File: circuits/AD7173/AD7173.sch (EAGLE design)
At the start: 32 parts, among them IC1 AD7173, IC2 ADP1720, IC3 ADP1720ARMZ-5, IC4 OPA2134D, IC6 OPA2725DGK

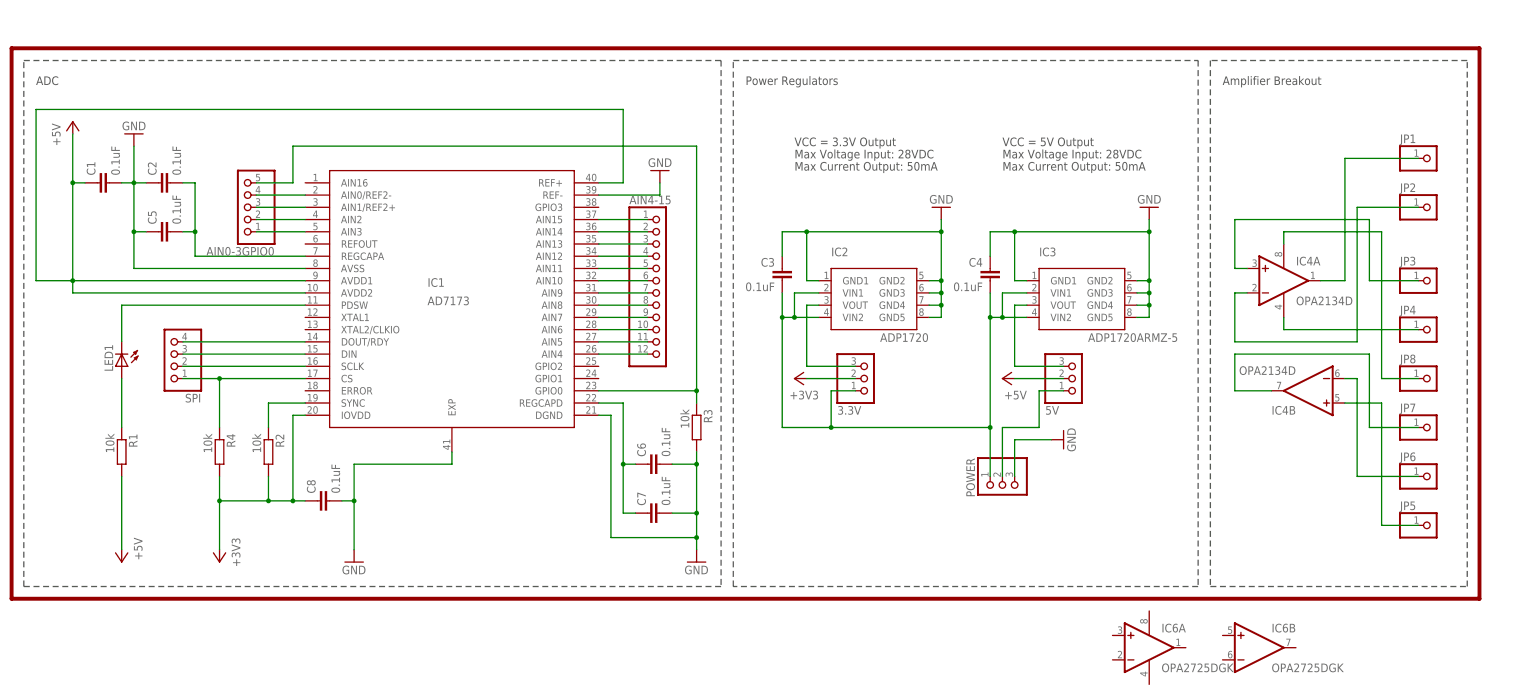
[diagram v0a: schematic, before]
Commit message: upadted AD7173 circuits
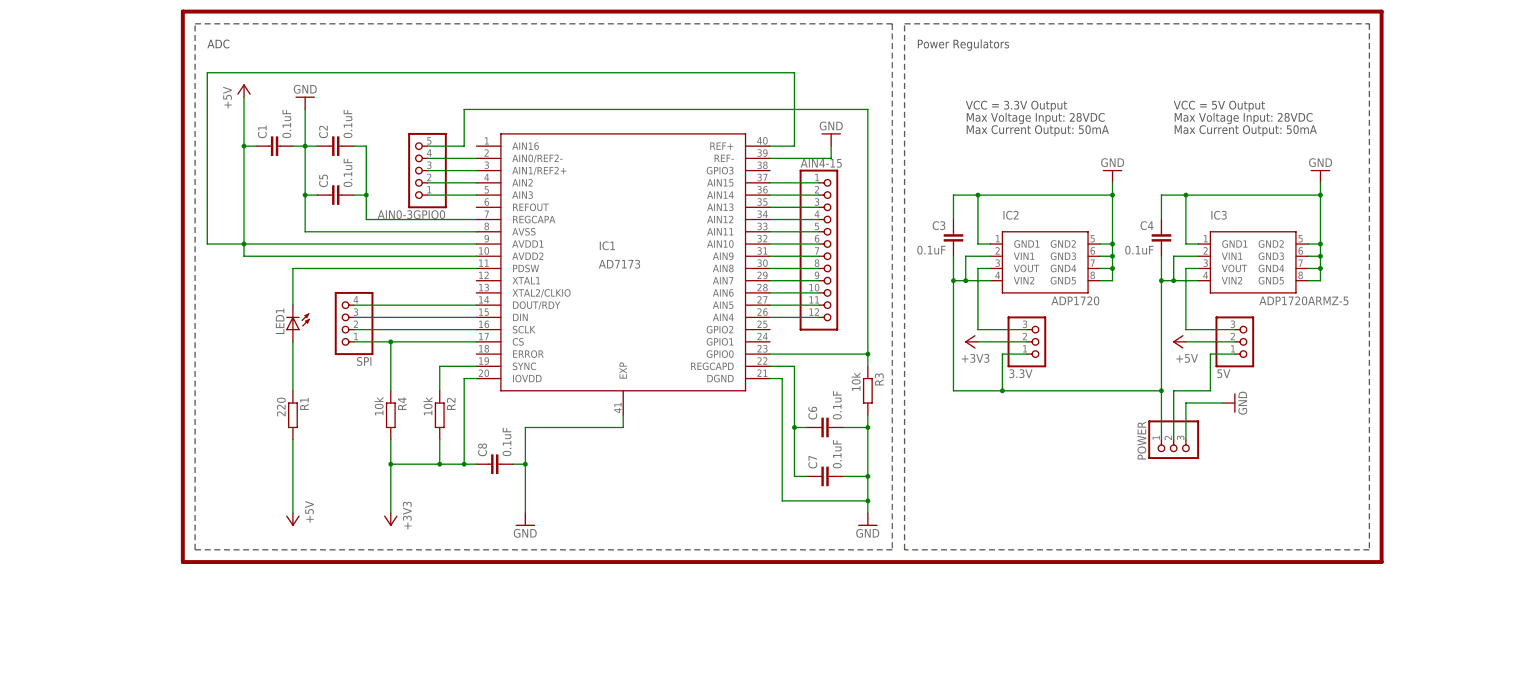
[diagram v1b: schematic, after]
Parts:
- removed IC4: OPA2134D, linear:OPA2134D
- removed IC6: OPA2725DGK, linear:OPA2725DGK
- removed JP1, JP2, JP3, JP4, JP5, JP6, JP7, JP8: (no value), pinhead:PINHD-1X1
- R1: value 10k -> 220
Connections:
- removed net N$31: IC4A.OUT, JP1.1
- removed net N$33: IC4A.-IN, JP2.1
- removed net N$34: IC4A.+IN, JP3.1
- removed net N$35: IC4P.V-, JP4.1
- removed net N$36: IC4B.+IN, JP5.1
- removed net N$37: IC4B.-IN, JP6.1
- removed net N$40: IC4B.OUT, JP7.1
- removed net N$41: IC4P.V+, JP8.1
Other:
- note removed: "Amplifier Breakout"
- moved on the sheet: 3.3V, 5V, AIN0-3GPIO0, AIN4-15, C1, C2, C3, C4, C5, C6, C7, C8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

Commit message: updated AD7173 circuit
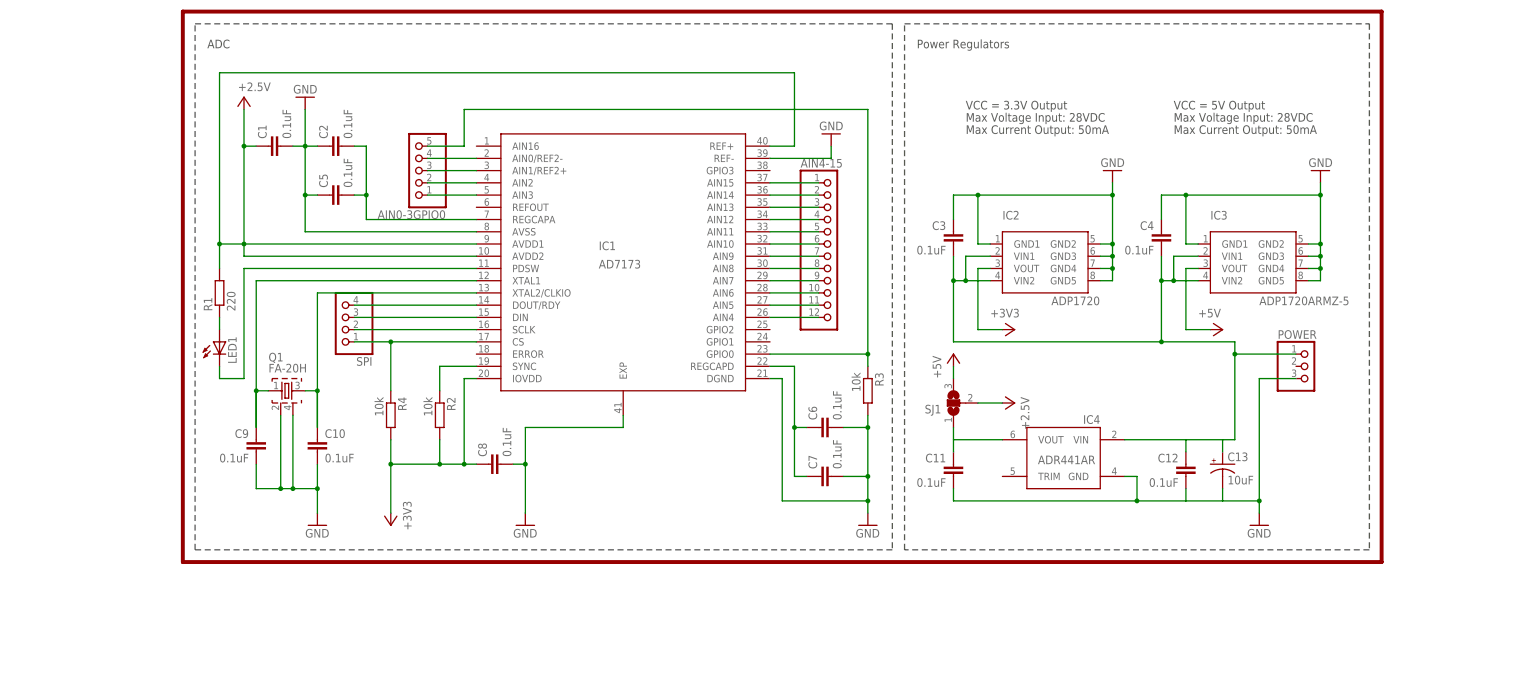
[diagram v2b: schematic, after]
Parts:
- removed 3.3V, 5V: (no value), pinhead:PINHD-1X3
- added C10, C11, C12, C9: 0.1uF, rcl:C-EUC0402
- added C13: 10uF, rcl:CPOL-USE1.8-4
- added IC4: ADR441AR, kblom:ADR441AR
- added Q1: FA-20H, crystal:FA-20H
- added SJ1: (no value), jumper:SJ2W
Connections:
- removed net N$30: 5V.3, IC3.VOUT
- new net V+: C1.1, IC1.AVDD1, IC1.AVDD2, IC1.REF+, R1.2, SJ1.2
- new net VIN: C12.1, C13.+, C3.2, C4.2, IC2.VIN1, IC2.VIN2, IC3.VIN1, IC3.VIN2, IC4.VIN, POWER.1
- net +3V3: now also IC2.VOUT; no longer 3.3V.2
- net +5V: now also IC3.VOUT, SJ1.3; no longer 5V.2, C1.1, IC1.AVDD1, IC1.AVDD2, IC1.REF+, R1.2
- net GND: now also C10.2, C11.2, C12.2, C13.-, C9.2, IC4.GND, Q1.2, Q1.4
- net N$22: now also C10.1, IC1.XTAL2/CLKIO, Q1.3; no longer 5V.1, POWER.2
- net N$27: now also C9.1, IC1.XTAL1, Q1.1; no longer 3.3V.3, IC2.VOUT
- net N$28: now also C11.1, IC4.VOUT, SJ1.1; no longer 3.3V.1, C3.2, C4.2, IC2.VIN1, IC2.VIN2, IC3.VIN1, IC3.VIN2, POWER.1
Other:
- moved on the sheet: LED1, POWER, R1

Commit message: updated AD7173 breakout board
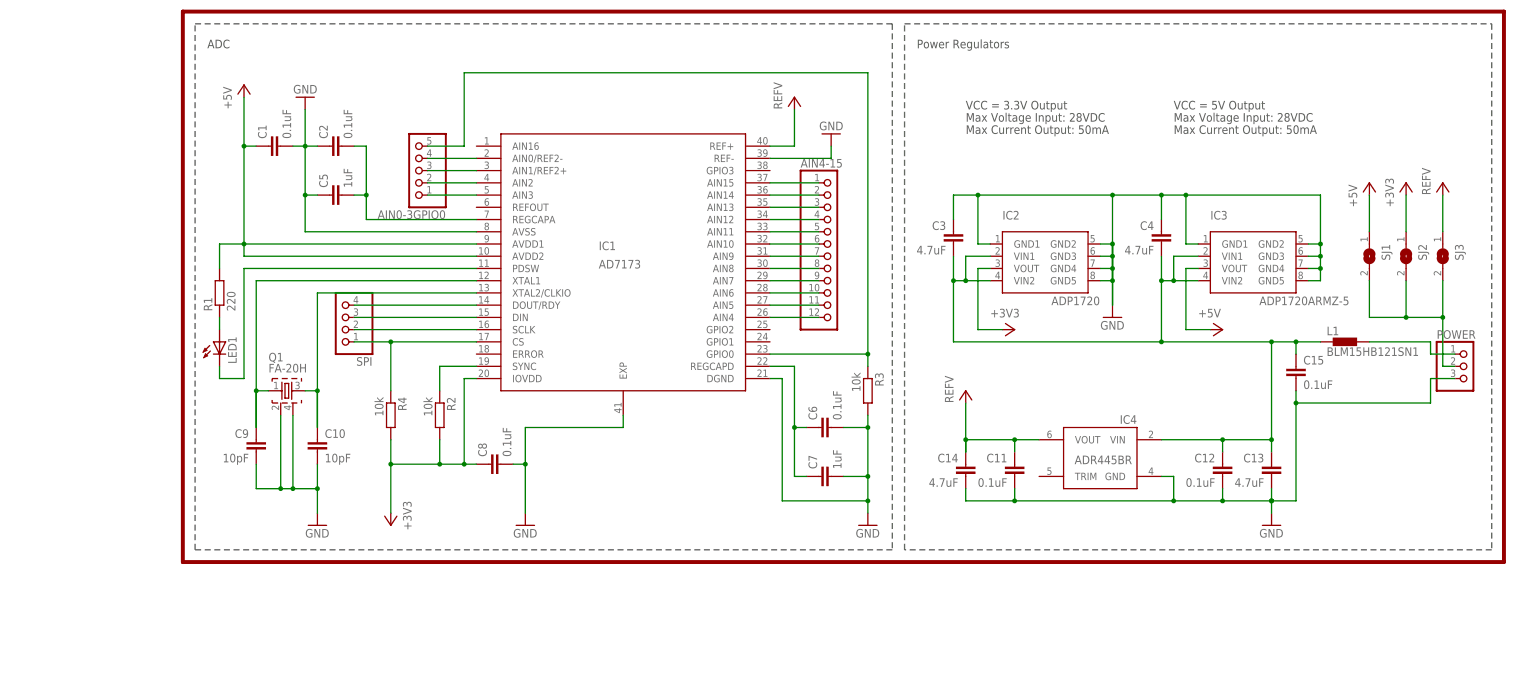
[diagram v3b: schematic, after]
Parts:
- added C14: 4.7uF, rcl:C-EUC0402
- added C15: 0.1uF, rcl:C-EUC0402
- added L1: BLM15HB121SN1, inductors:BLM15HB121SN1
- added SJ2, SJ3: (no value), jumper:SJ
- C10, C9: value 0.1uF -> 10pF
- C13: value 10uF -> 4.7uF; device rcl:CPOL-USE1.8-4 -> rcl:C-EUC0402
- C3, C4: value 0.1uF -> 4.7uF
- C5, C7: value 0.1uF -> 1uF
- IC4: value ADR441AR -> ADR445BR; device kblom:ADR441AR -> kblom:ADR445BR
- SJ1: device jumper:SJ2W -> jumper:SJ
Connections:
- removed net V+: C1.1, IC1.AVDD1, IC1.AVDD2, IC1.REF+, R1.2, SJ1.2
- new net N$30: L1.2, POWER.1
- new net VCC: C11.1, C14.1, IC1.REF+, IC4.VOUT, SJ3.1
- net +3V3: now also SJ2.1
- net +5V: now also C1.1, IC1.AVDD1, IC1.AVDD2, R1.2, SJ1.1; no longer SJ1.3
- net GND: now also C13.2, C14.2, C15.2; no longer C13.-
- net N$28: now also POWER.2, SJ1.2, SJ2.2, SJ3.2; no longer C11.1, IC4.VOUT, SJ1.1
- net VIN: now also C13.1, C15.1, L1.1; no longer C13.+, POWER.1
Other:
- moved on the sheet: C11, C12, IC4, POWER

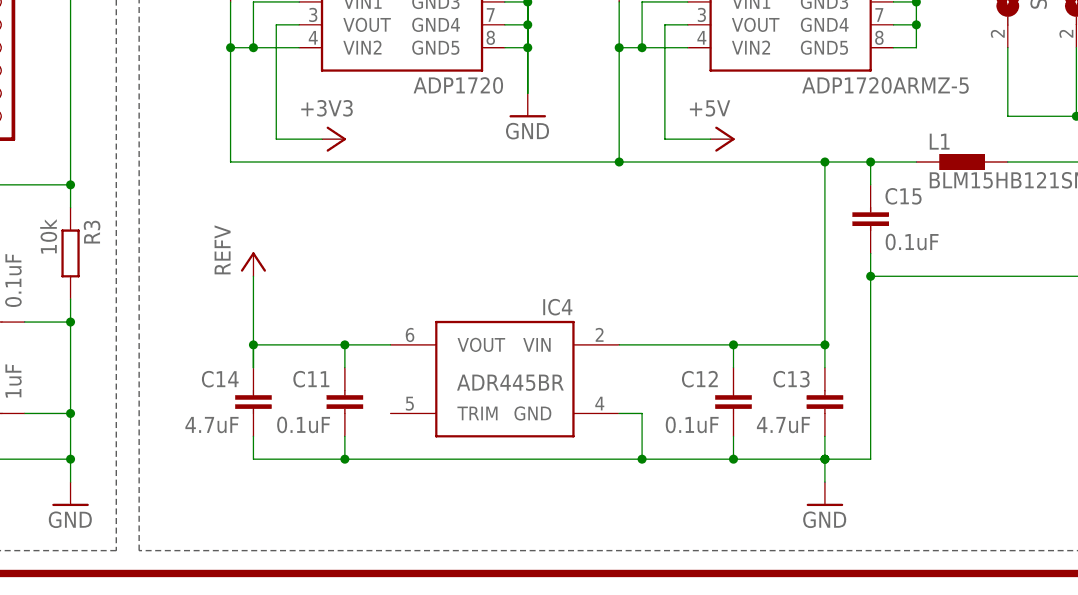
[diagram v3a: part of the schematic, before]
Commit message: updated AD7173 breakout board
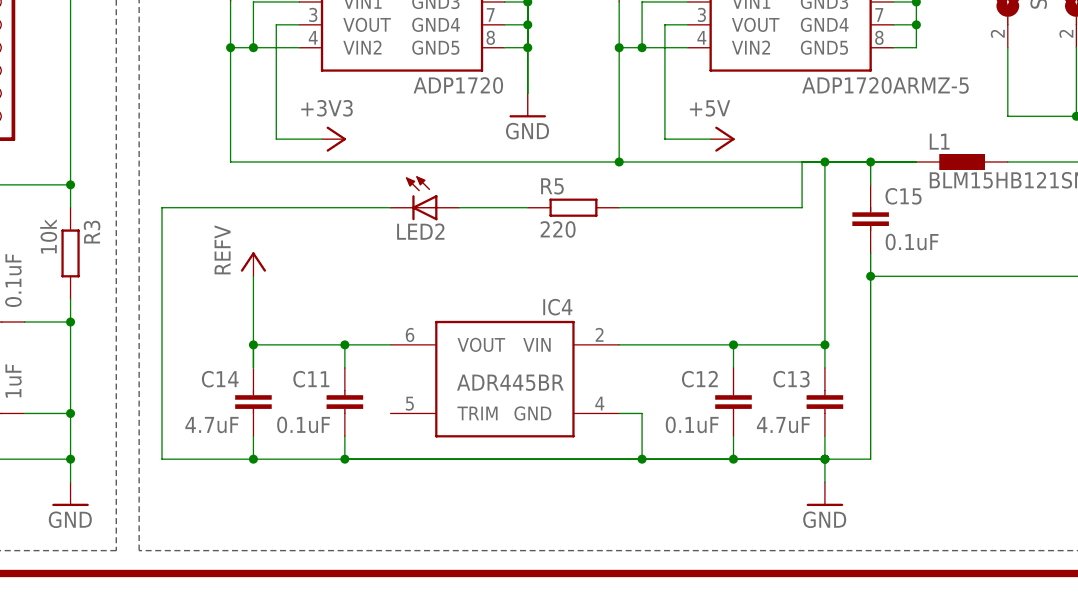
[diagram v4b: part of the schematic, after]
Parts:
- added LED2: (no value), led:LEDCHIP-LED0603
- added R5: 220, rcl:R-EU_R0402
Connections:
- new net N$31: LED2.A, R5.1
- net GND: now also LED2.C
- net VIN: now also R5.2
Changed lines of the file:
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@@
 <part name="+3V3" library="supply1" deviceset="+3V3" device=""/>
 <part name="P+6" library="supply1" deviceset="VCC" device="" value="REFV"/>
+<part name="LED2" library="led" deviceset="LED" device="CHIP-LED0603"/>
+<part name="R5" library="rcl" deviceset="R-EU_" device="R0402" value="220"/>
 </parts>
 <sheets>
@@
 <instance part="+3V3" gate="G$1" x="254" y="78.74"/>
 <instance part="P+6" gate="VCC" x="261.62" y="78.74"/>
+<instance part="LED2" gate="G$1" x="182.88" y="40.64" rot="R270"/>
+<instance part="R5" gate="G$1" x="198.12" y="40.64"/>
 </instances>
 <busses>
@@
 <wire x1="215.9" y1="12.7" x2="226.06" y2="12.7" width="0.1524" layer="91"/>
 <wire x1="226.06" y1="15.24" x2="226.06" y2="12.7" width="0.1524" layer="91"/>
-<wire x1="226.06" y1="12.7" x2="226.06" y2="10.16" width="0.1524" layer="91"/>
 <pinref part="C13" gate="G$1" pin="2"/>
 <junction x="215.9" y="12.7"/>
@@
 <wire x1="231.14" y1="33.02" x2="231.14" y2="35.56" width="0.1524" layer="91"/>
 <junction x="172.72" y="12.7"/>
+<pinref part="LED2" gate="G$1" pin="C"/>
+<wire x1="177.8" y1="40.64" x2="152.4" y2="40.64" width="0.1524" layer="91"/>
+<wire x1="152.4" y1="40.64" x2="152.4" y2="12.7" width="0.1524" layer="91"/>
+<wire x1="152.4" y1="12.7" x2="162.56" y2="12.7" width="0.1524" layer="91"/>
+<wire x1="172.72" y1="12.7" x2="226.06" y2="12.7" width="0.1524" layer="91"/>
+<wire x1="226.06" y1="12.7" x2="226.06" y2="10.16" width="0.1524" layer="91"/>
+<junction x="162.56" y="12.7"/>
 </segment>
 <segment>
@@
 <junction x="226.06" y="45.72"/>
 <junction x="231.14" y="45.72"/>
+<wire x1="236.22" y1="45.72" x2="223.52" y2="45.72" width="0.1524" layer="91"/>
+<wire x1="223.52" y1="45.72" x2="223.52" y2="40.64" width="0.1524" layer="91"/>
+<pinref part="R5" gate="G$1" pin="2"/>
+<wire x1="223.52" y1="40.64" x2="203.2" y2="40.64" width="0.1524" layer="91"/>
 </segment>
 </net>
@@
 </segment>
 </net>
+<net name="N$31" class="0">
+<segment>
+<pinref part="LED2" gate="G$1" pin="A"/>
+<pinref part="R5" gate="G$1" pin="1"/>
+<wire x1="193.04" y1="40.64" x2="185.42" y2="40.64" width="0.1524" layer="91"/>
+</segment>
+</net>

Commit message: upadted AD7173 breakout board
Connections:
- net N$30: now also R5.2
- net VIN: no longer R5.2
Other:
- moved on the sheet: C15, L1
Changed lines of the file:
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@@
 <instance part="P+2" gate="VCC" x="127" y="96.52"/>
 <instance part="P+1" gate="VCC" x="162.56" y="35.56"/>
-<instance part="L1" gate="G$1" x="241.3" y="45.72"/>
-<instance part="C15" gate="G$1" x="231.14" y="40.64"/>
+<instance part="L1" gate="G$1" x="241.3" y="43.18"/>
+<instance part="C15" gate="G$1" x="231.14" y="38.1"/>
 <instance part="P+4" gate="1" x="12.7" y="99.06"/>
 <instance part="SJ1" gate="1" x="246.38" y="63.5" rot="R270"/>
@@
 <pinref part="GND5" gate="1" pin="GND"/>
 <wire x1="226.06" y1="12.7" x2="231.14" y2="12.7" width="0.1524" layer="91"/>
-<wire x1="231.14" y1="12.7" x2="231.14" y2="33.02" width="0.1524" layer="91"/>
+<wire x1="231.14" y1="12.7" x2="231.14" y2="30.48" width="0.1524" layer="91"/>
 <pinref part="IC4" gate="G$1" pin="GND"/>
 <pinref part="C11" gate="G$1" pin="2"/>
@@
 <wire x1="162.56" y1="12.7" x2="172.72" y2="12.7" width="0.1524" layer="91"/>
 <wire x1="172.72" y1="12.7" x2="172.72" y2="15.24" width="0.1524" layer="91"/>
-<junction x="231.14" y="33.02"/>
+<junction x="231.14" y="30.48"/>
 <wire x1="264.16" y1="38.1" x2="259.08" y2="38.1" width="0.1524" layer="91"/>
-<wire x1="259.08" y1="38.1" x2="259.08" y2="33.02" width="0.1524" layer="91"/>
+<wire x1="259.08" y1="38.1" x2="259.08" y2="30.48" width="0.1524" layer="91"/>
 <pinref part="C15" gate="G$1" pin="2"/>
-<wire x1="259.08" y1="33.02" x2="231.14" y2="33.02" width="0.1524" layer="91"/>
-<wire x1="231.14" y1="33.02" x2="231.14" y2="35.56" width="0.1524" layer="91"/>
+<wire x1="259.08" y1="30.48" x2="231.14" y2="30.48" width="0.1524" layer="91"/>
+<wire x1="231.14" y1="30.48" x2="231.14" y2="33.02" width="0.1524" layer="91"/>
 <junction x="172.72" y="12.7"/>
 <pinref part="LED2" gate="G$1" pin="C"/>
@@
 <pinref part="C3" gate="G$1" pin="2"/>
 <wire x1="160.02" y1="63.5" x2="160.02" y2="58.42" width="0.1524" layer="91"/>
+<wire x1="226.06" y1="43.18" x2="226.06" y2="45.72" width="0.1524" layer="91"/>
 <wire x1="226.06" y1="45.72" x2="203.2" y2="45.72" width="0.1524" layer="91"/>
 <wire x1="203.2" y1="45.72" x2="160.02" y2="45.72" width="0.1524" layer="91"/>
@@
 <junction x="162.56" y="58.42"/>
 <junction x="203.2" y="58.42"/>
-<wire x1="226.06" y1="25.4" x2="226.06" y2="45.72" width="0.1524" layer="91"/>
+<wire x1="226.06" y1="25.4" x2="226.06" y2="43.18" width="0.1524" layer="91"/>
 <pinref part="C13" gate="G$1" pin="1"/>
 <junction x="226.06" y="25.4"/>
 <junction x="215.9" y="25.4"/>
 <pinref part="L1" gate="G$1" pin="1"/>
-<wire x1="231.14" y1="45.72" x2="226.06" y2="45.72" width="0.1524" layer="91"/>
+<wire x1="231.14" y1="43.18" x2="226.06" y2="43.18" width="0.1524" layer="91"/>
 <wire x1="226.06" y1="25.4" x2="226.06" y2="22.86" width="0.1524" layer="91"/>
 <pinref part="C15" gate="G$1" pin="1"/>
-<wire x1="236.22" y1="45.72" x2="231.14" y2="45.72" width="0.1524" layer="91"/>
-<wire x1="231.14" y1="45.72" x2="231.14" y2="43.18" width="0.1524" layer="91"/>
-<junction x="226.06" y="45.72"/>
-<junction x="231.14" y="45.72"/>
-<wire x1="236.22" y1="45.72" x2="223.52" y2="45.72" width="0.1524" layer="91"/>
-<wire x1="223.52" y1="45.72" x2="223.52" y2="40.64" width="0.1524" layer="91"/>
-<pinref part="R5" gate="G$1" pin="2"/>
-<wire x1="223.52" y1="40.64" x2="203.2" y2="40.64" width="0.1524" layer="91"/>
+<wire x1="236.22" y1="43.18" x2="231.14" y2="43.18" width="0.1524" layer="91"/>
+<wire x1="231.14" y1="43.18" x2="231.14" y2="40.64" width="0.1524" layer="91"/>
+<junction x="226.06" y="43.18"/>
+<junction x="231.14" y="43.18"/>
 </segment>
 </net>
@@
 <pinref part="L1" gate="G$1" pin="2"/>
 <wire x1="264.16" y1="43.18" x2="259.08" y2="43.18" width="0.1524" layer="91"/>
-<wire x1="259.08" y1="43.18" x2="259.08" y2="45.72" width="0.1524" layer="91"/>
-<wire x1="259.08" y1="45.72" x2="246.38" y2="45.72" width="0.1524" layer="91"/>
-</segment>
-</net>
+<wire x1="259.08" y1="43.18" x2="246.38" y2="43.18" width="0.1524" layer="91"/>
+<wire x1="259.08" y1="43.18" x2="259.08" y2="48.26" width="0.1524" layer="91"/>
+<wire x1="259.08" y1="48.26" x2="220.98" y2="48.26" width="0.1524" layer="91"/>
+<wire x1="220.98" y1="48.26" x2="220.98" y2="40.64" width="0.1524" layer="91"/>
+<pinref part="R5" gate="G$1" pin="2"/>
+<wire x1="220.98" y1="40.64" x2="203.2" y2="40.64" width="0.1524" layer="91"/>
+<junction x="259.08" y="43.18"/>
+</segment>
+</net>
